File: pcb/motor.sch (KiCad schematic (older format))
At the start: 5 parts, among them IC6 DRV8835, P6 MOTOR

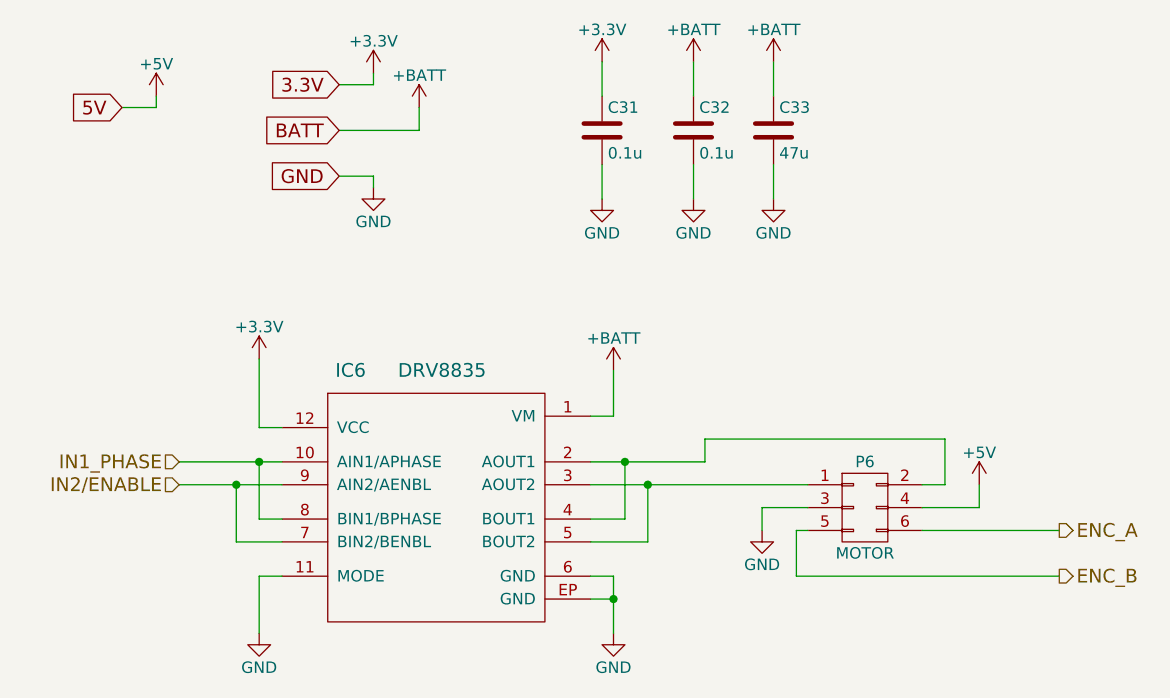
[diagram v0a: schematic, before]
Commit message: 回路図を修正 ・赤外線LEDの発光回路にpull down抵抗を追加 ・赤外線LEDの発光回路の電流制限抵抗の値を変更
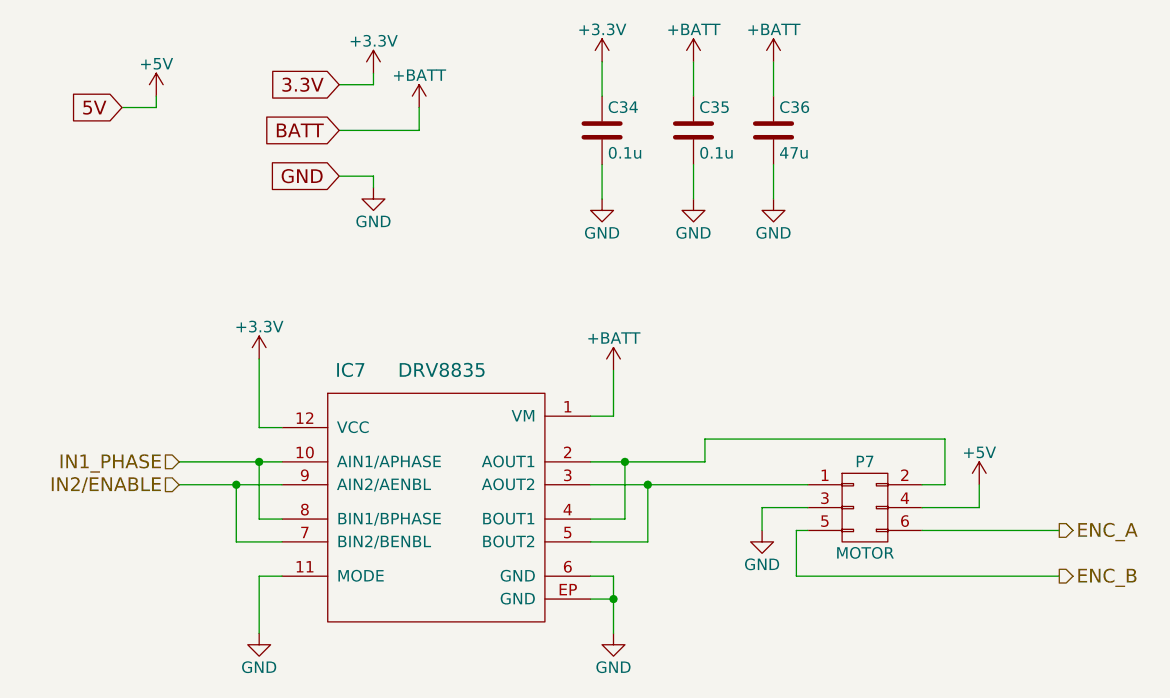
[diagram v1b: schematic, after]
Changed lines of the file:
@@
 AR Path="/57CD848F/57DFB122" Ref="IC6"  Part="1"
 AR Path="/57E4ED65/57DFB122" Ref="IC7"  Part="1"
-F 0 "IC6" H 5350 4650 60  0000 C CNN
+F 0 "IC7" H 5350 4650 60  0000 C CNN
 F 1 "DRV8835" H 5750 4650 60  0000 C CNN
 F 2 "micromouse2016:DRV8835" H 5700 4100 60  0001 C CNN
@@
 AR Path="/57CD848F/57DFB8D1" Ref="C31"  Part="1"
 AR Path="/57E4ED65/57DFB8D1" Ref="C34"  Part="1"
-F 0 "C31" H 6475 2600 50  0000 L CNN
+F 0 "C34" H 6475 2600 50  0000 L CNN
 F 1 "0.1u" H 6475 2400 50  0000 L CNN
 F 2 "Capacitors_SMD:C_0603" H 6488 2350 50  0001 C CNN
@@
 AR Path="/57CD848F/57DFB925" Ref="C32"  Part="1"
 AR Path="/57E4ED65/57DFB925" Ref="C35"  Part="1"
-F 0 "C32" H 6875 2600 50  0000 L CNN
+F 0 "C35" H 6875 2600 50  0000 L CNN
 F 1 "0.1u" H 6875 2400 50  0000 L CNN
 F 2 "Capacitors_SMD:C_0603" H 6888 2350 50  0001 C CNN
@@
 AR Path="/57CD848F/57DFD438" Ref="P6"  Part="1"
 AR Path="/57E4ED65/57DFD438" Ref="P7"  Part="1"
-F 0 "P6" H 7600 4350 50  0000 C CNN
+F 0 "P7" H 7600 4350 50  0000 C CNN
 F 1 "MOTOR" H 7600 3950 50  0000 C CNN
 F 2 "Pin_Headers:Pin_Header_Straight_2x03" H 7600 2950 50  0001 C CNN
@@
 AR Path="/57CD848F/57E4E293" Ref="C33"  Part="1"
 AR Path="/57E4ED65/57E4E293" Ref="C36"  Part="1"
-F 0 "C33" H 7225 2600 50  0000 L CNN
+F 0 "C36" H 7225 2600 50  0000 L CNN
 F 1 "47u" H 7225 2400 50  0000 L CNN
 F 2 "Capacitors_SMD:C_1206" H 7238 2350 50  0001 C CNN
